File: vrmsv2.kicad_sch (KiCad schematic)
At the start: 5 parts

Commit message: Redo of placement
Really like this attempt
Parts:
- D3: footprint Diode_SMD:D_SOD-323 -> Diode_SMD:D_SOD-323_HandSoldering
- D4: footprint Diode_SMD:D_SMA -> Diode_SMD:D_SMA_Handsoldering
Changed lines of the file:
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@@
       (effects (font (size 1.27 1.27)) hide)
     )
-    (property "Footprint" "Diode_SMD:D_SMA" (id 2) (at 114.3 82.55 0)
+    (property "Footprint" "Diode_SMD:D_SMA_Handsoldering" (id 2) (at 114.3 82.55 0)
       (effects (font (size 1.27 1.27)) hide)
     )
@@
       (effects (font (size 1.27 1.27)) (justify left))
     )
-    (property "Footprint" "Diode_SMD:D_SOD-323" (id 2) (at 104.14 86.36 0)
+    (property "Footprint" "Diode_SMD:D_SOD-323_HandSoldering" (id 2) (at 104.14 86.36 0)
       (effects (font (size 1.27 1.27)) hide)
     )

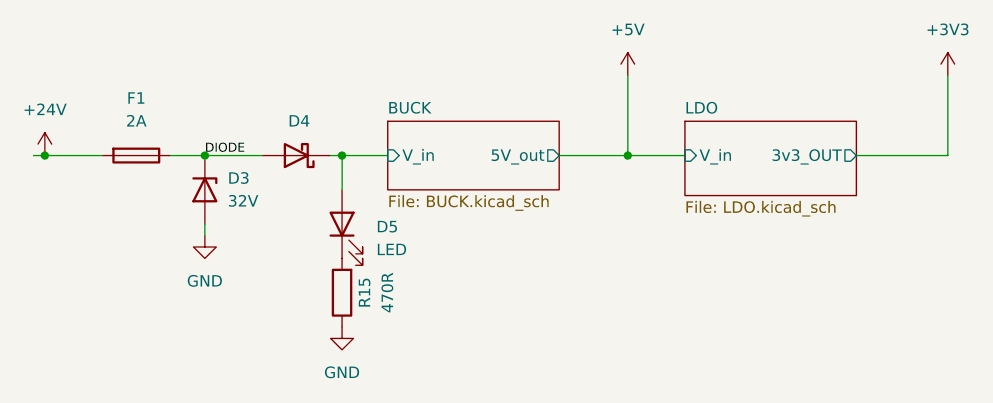
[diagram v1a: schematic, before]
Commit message: Added 0 Ohm resistor between shield (grounded)
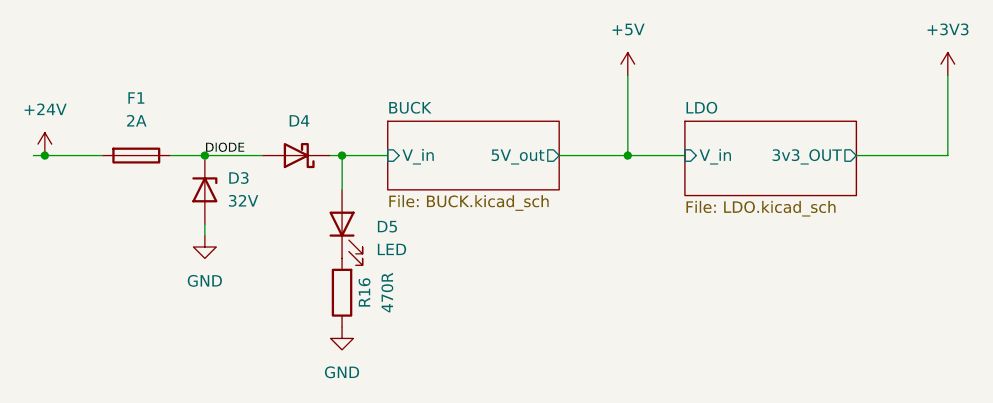
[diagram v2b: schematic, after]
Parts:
- renumbered R15 to R16
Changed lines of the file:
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@@
   (symbol (lib_id "power:+3V3") (at 186.69 73.66 0) (unit 1)
     (in_bom yes) (on_board yes) (fields_autoplaced)
-    (property "Reference" "#PWR044" (id 0) (at 186.69 77.47 0)
+    (property "Reference" "#PWR050" (id 0) (at 186.69 77.47 0)
       (effects (font (size 1.27 1.27)) hide)
     )
@@
   (symbol (lib_id "power:+5V") (at 151.13 73.66 0) (unit 1)
     (in_bom yes) (on_board yes) (fields_autoplaced)
-    (property "Reference" "#PWR043" (id 0) (at 151.13 77.47 0)
+    (property "Reference" "#PWR049" (id 0) (at 151.13 77.47 0)
       (effects (font (size 1.27 1.27)) hide)
     )
@@
   (symbol (lib_id "power:GND") (at 104.14 91.44 0) (unit 1)
     (in_bom yes) (on_board yes) (fields_autoplaced)
-    (property "Reference" "#PWR041" (id 0) (at 104.14 97.79 0)
+    (property "Reference" "#PWR047" (id 0) (at 104.14 97.79 0)
       (effects (font (size 1.27 1.27)) hide)
     )
@@
   (symbol (lib_id "power:+24V") (at 86.36 82.55 0) (unit 1)
     (in_bom yes) (on_board yes) (fields_autoplaced)
-    (property "Reference" "#PWR040" (id 0) (at 86.36 86.36 0)
+    (property "Reference" "#PWR046" (id 0) (at 86.36 86.36 0)
       (effects (font (size 1.27 1.27)) hide)
     )
@@
   (symbol (lib_id "Device:R") (at 119.38 97.79 180) (unit 1)
     (in_bom yes) (on_board yes)
-    (property "Reference" "R15" (id 0) (at 121.92 97.79 90))
+    (property "Reference" "R16" (id 0) (at 121.92 97.79 90))
     (property "Value" "470R" (id 1) (at 124.46 97.79 90))
     (property "Footprint" "Resistor_SMD:R_0603_1608Metric_Pad0.98x0.95mm_HandSolder" (id 2) (at 121.158 97.79 90)
@@
   (symbol (lib_id "power:GND") (at 119.38 101.6 0) (unit 1)
     (in_bom yes) (on_board yes) (fields_autoplaced)
-    (property "Reference" "#PWR042" (id 0) (at 119.38 107.95 0)
+    (property "Reference" "#PWR048" (id 0) (at 119.38 107.95 0)
       (effects (font (size 1.27 1.27)) hide)
     )
